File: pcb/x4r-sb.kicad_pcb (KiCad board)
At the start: 2 copper layers, 36 x 36 mm, 30 parts, among them P1 CONN_01X04, P10 CONN_01X01, P2 CONN_02X06, P3 CONN_01X02, P5 CONN_01X01, P7 CONN_01X01, P8 CONN_01X01, P9 CONN_01X01, Q1 Q_NMOS_GSD, U1 74LS86

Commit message: Unknown changes to x4r
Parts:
- removed the G*** at (165.0, 107.9) (x2)
- added F1: 1mm, macrofab:Fiducial, F.Cu at (131.4, 120.7)
- added F2: 1mm, macrofab:Fiducial, F.Cu at (131.3, 95.4)
- added F3: 1mm, macrofab:Fiducial, F.Cu at (160.7, 91.2)
- added F4: 1mm, macrofab:Fiducial, B.Cu at (131.4, 120.7)
- added F5: 1mm, macrofab:Fiducial, B.Cu at (131.3, 95.4)
- added F6: 1mm, macrofab:Fiducial, B.Cu at (164.7, 95.2)
- added G***: LOGO, flightstack:flightstack_thin-8mm, B.Cu at (164.9, 108.1)
- added G***: LOGO, flightstack:flightstack_thin-8mm, F.Cu at (164.9, 107.9)
- added G***: OSHW, oshw:oshw-2mm, B.Cu at (152.0, 91.3)
- added G***: LOGO, chickadee:chickadee_2mm_fcu, B.Cu at (147.7, 91.3)
- added G***: OSHW, oshw:oshw-3mm, F.Cu at (164.2, 118.7)
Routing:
- net GND: track 144.2 -> 142.2 mm
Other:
- board text added: "ckd.tech/x4r-sb/v3"
- board text removed: "ckd.tech/x4r-sb/v2"

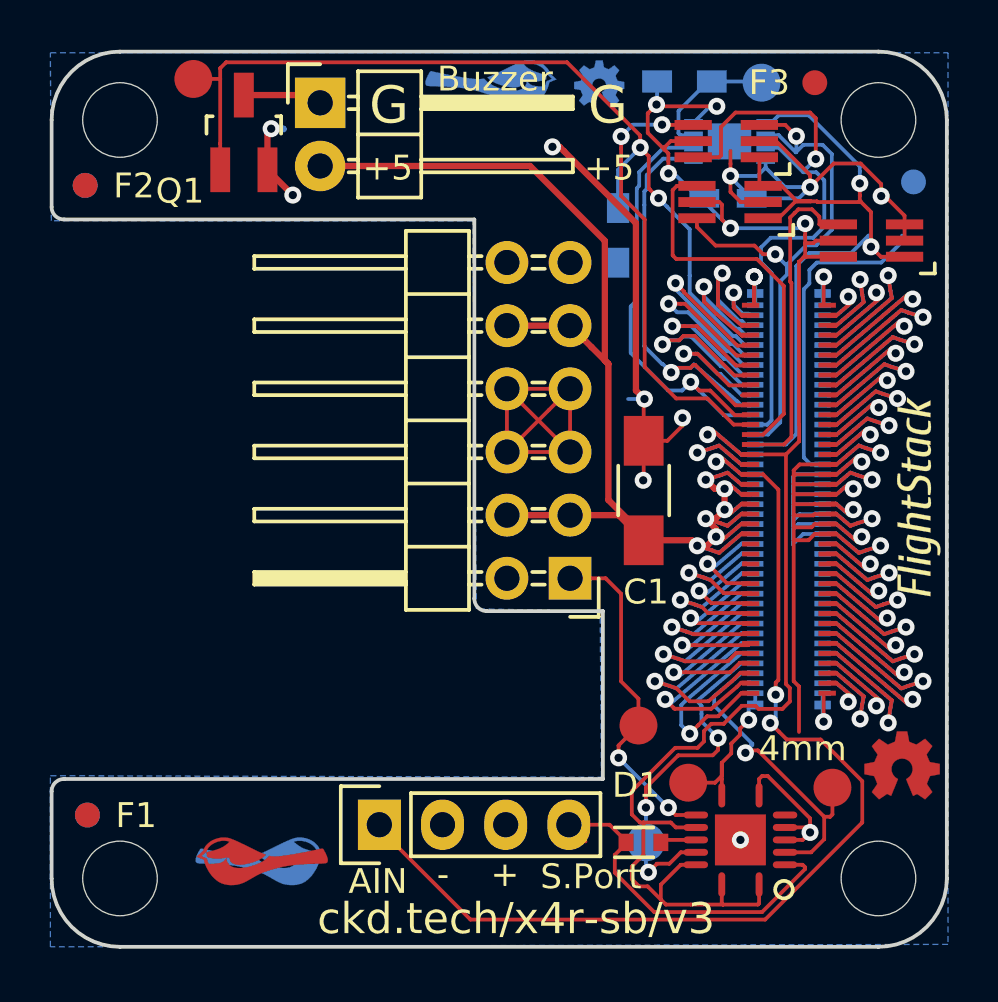
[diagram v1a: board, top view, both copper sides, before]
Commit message: Rebrand everything to Polystack and increment versions.
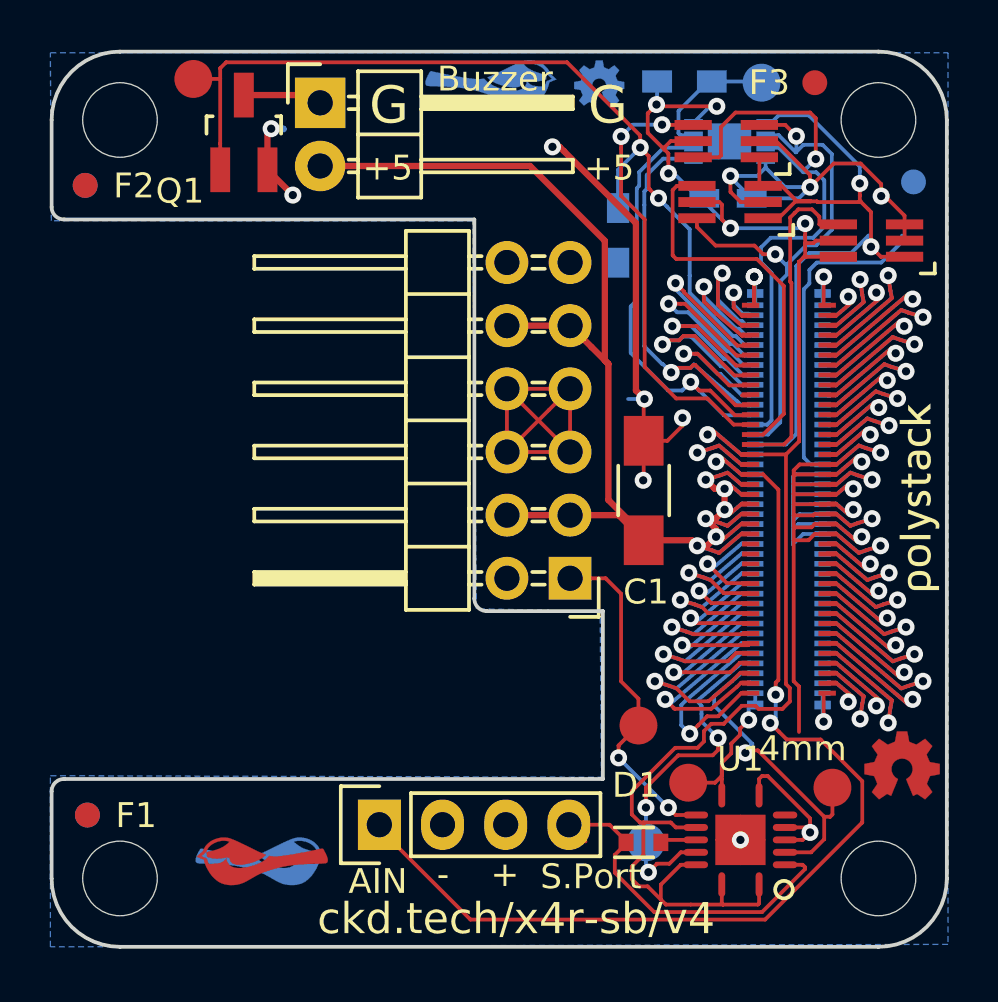
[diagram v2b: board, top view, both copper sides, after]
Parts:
- removed the G*** at (164.9, 108.1)
- removed the G*** at (164.9, 107.9)
- added svg2mod: G***, polystack:polystack-medium-0.4, B.Cu at (164.9, 107.9)
- added svg2mod: G***, polystack:polystack-medium-0.4, F.Cu at (164.9, 107.9)
- U1: footprint QFN-14-3.5x3.5mm -> ti-gate:QFN-14-3.5x3.5mm
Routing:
- net GND: track 142.2 -> 141.2 mm
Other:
- rule pad_to_mask_clearance: 0.2 -> 0.0762
- board text added: "ckd.tech/x4r-sb/v4"
- board text removed: "ckd.tech/x4r-sb/v3"

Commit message: Update polystack logo to bold variant and bump version number.
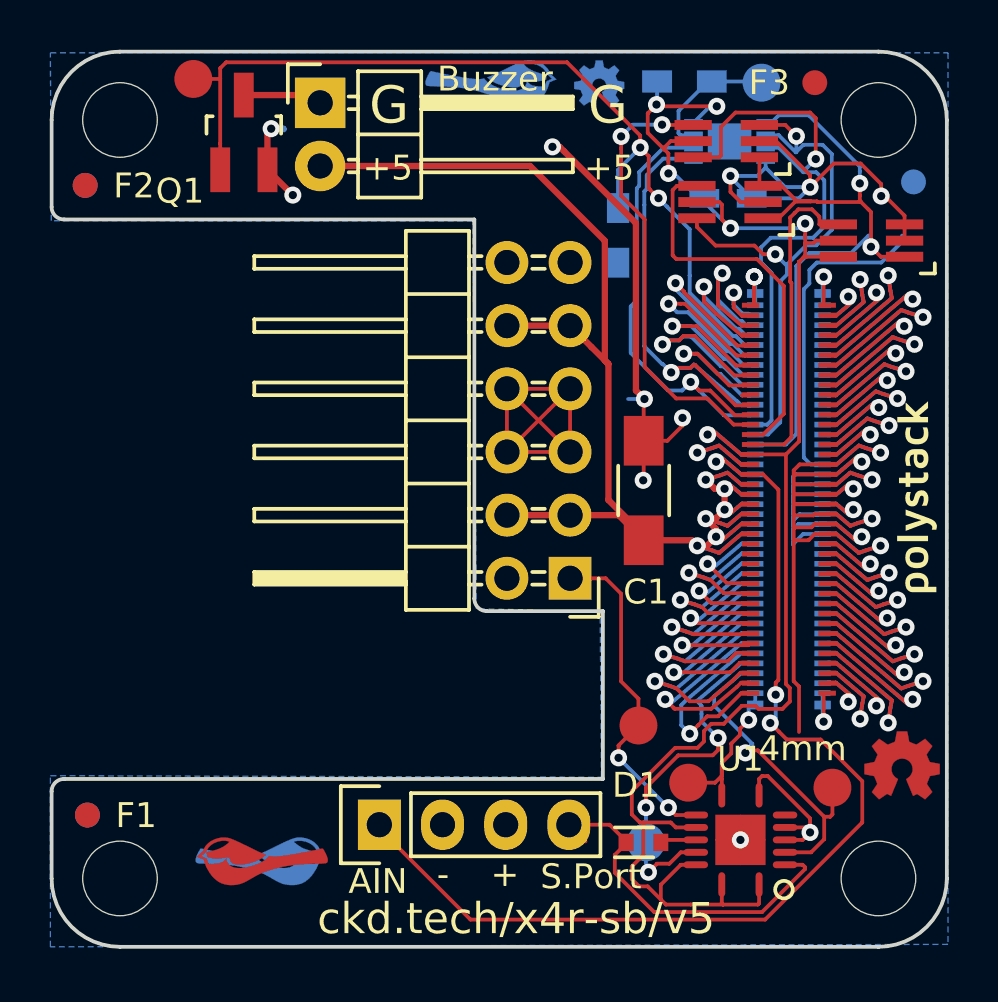
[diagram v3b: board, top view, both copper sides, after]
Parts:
- svg2mod (x2): footprint polystack:polystack-medium-0.4 -> polystack:polystack-bold-0.4
- moved svg2mod 0.10 mm to (164.8, 107.9) (x2)
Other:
- board text added: "ckd.tech/x4r-sb/v5"
- board text removed: "ckd.tech/x4r-sb/v4"

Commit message: Add license information to many files. PCB design files are CC-BY and code is MIT license.
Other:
- board text added: "Copyright 2016 Chickadee Tech LLC, <add attributions here> This work is licensed under the Creative Commons Attribution 4.0 International License. To view a copy of this license, visit http://creativecommons.org/licenses/by/4.0/ or send a letter to Creative Commons, PO Box 1866, Mountain View, CA 94042, USA."
- board text added: "Remove all Chickadee Tech LLC trademarks before making your own board. The Chickadee logo and Polystack logo are owned by Chickadee Tech LLC. You may license the Polystack logo for free by emailing support@chickadee.tech and receiving express written permission from Chickadee Tech LLC."
- board text added: "The gear logo is a mark designating open source hardware. Remove it if your design does not comply with the open source hardware definition."
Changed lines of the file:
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@@
     (links 159)
     (no_connects 0)
-    (area 118.127143 74.1 214.166667 178)
+    (area 67.31 74.1 280.760001 191.8)
     (thickness 1.6)
-    (drawings 53)
+    (drawings 64)
     (tracks 1129)
     (zones 0)
@@
     (40 Dwgs.User user)
     (41 Cmts.User user)
-    (42 Eco1.User user hide)
-    (43 Eco2.User user hide)
+    (42 Eco1.User user)
+    (43 Eco2.User user)
     (44 Edge.Cuts user)
     (45 Margin user)
@@
       (xy 2.990233 -0.444493)) (layer B.SilkS) (width 0))
   )
+  (gr_line (start 177.63 115.9) (end 166.14 118.1) (layer Cmts.User) (width 0.2))
+  (gr_line (start 177.63 115.78) (end 153.54 92.3) (layer Cmts.User) (width 0.2))
+  (gr_text "The gear logo is a mark designating open\nsource hardware. Remove it if your design\ndoes not comply with the open source\nhardware definition.\n" (at 178.37 116.02) (layer Cmts.User)
+    (effects (font (size 1.5 1.5) (thickness 0.3)) (justify left))
+  )
+  (gr_line (start 108.84 107.79) (end 135.81 119.99) (layer Cmts.User) (width 0.2))
+  (gr_line (start 109.14 107.99) (end 160.41 107.49) (layer Cmts.User) (width 0.2))
+  (gr_line (start 109.04 107.79) (end 144.86 93.32) (layer Cmts.User) (width 0.2))
+  (gr_circle (center 164.74 107.99) (end 166.51 111.82) (layer Cmts.User) (width 0.2))
+  (gr_circle (center 147.71 91.06) (end 150.47 92.63) (layer Cmts.User) (width 0.2))
+  (gr_circle (center 138.37 122.45) (end 141.02 124.32) (layer Cmts.User) (width 0.2))
+  (gr_text "Remove all Chickadee Tech LLC trademarks\nbefore making your own board. The\nChickadee logo and Polystack logo\nare owned by Chickadee Tech LLC.\n\nYou may license the Polystack logo for\nfree by emailing support@chickadee.tech\nand receiving express written permission\nfrom Chickadee Tech LLC." (at 67.46 109.46) (layer Cmts.User)
+    (effects (font (size 1.5 1.5) (thickness 0.3)) (justify left))
+  )
+  (gr_text "Copyright 2016 Chickadee Tech LLC, <add attributions here>\n\nThis work is licensed under the Creative Commons Attribution 4.0 International License.\nTo view a copy of this license, visit http://creativecommons.org/licenses/by/4.0/\nor send a letter to Creative Commons, PO Box 1866, Mountain View, CA 94042, USA." (at 179.11 173.75) (layer Cmts.User)
+    (effects (font (size 1.5 1.5) (thickness 0.3)) (justify left))
+  )
   (gr_text +5 (at 152.42 94.68) (layer F.SilkS)
     (effects (font (size 1 1) (thickness 0.15)))
@@
   (gr_line (start 166 92.75) (end 166 123.25) (angle 90) (layer Edge.Cuts) (width 0.15))
   (gr_line (start 132.75 90) (end 163.25 90) (angle 90) (layer Edge.Cuts) (width 0.15))
-  (gr_text x4r-sb (at 187.25 174.25) (layer Cmts.User)
-    (effects (font (size 5 5) (thickness 0.5)) (justify left))
+  (gr_text x4r-sb (at 187.08 189.45) (layer Cmts.User)
+    (effects (font (size 3 3) (thickness 0.5)) (justify left))
   )
   (segment (start 162.95 97.849974) (end 162.95 96.45) (width 0.1524) (layer F.Cu) (net 1))
